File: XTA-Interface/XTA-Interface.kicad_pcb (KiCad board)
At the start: 2 copper layers, 99.9 x 99.9 mm, 19 parts, among them J1 XTA_CONNECTOR_0, J2 Drive Power, J3 Bus_ISA_8bit, J4 Addresses, J5 Addresses, J6 LEDs, J7 XTA_CONNECTOR_1, U1 BIOS FLASH, U2 74HCT245, U3 ATF/GAL16V8-15, U4 ATF/GAL16V8-15

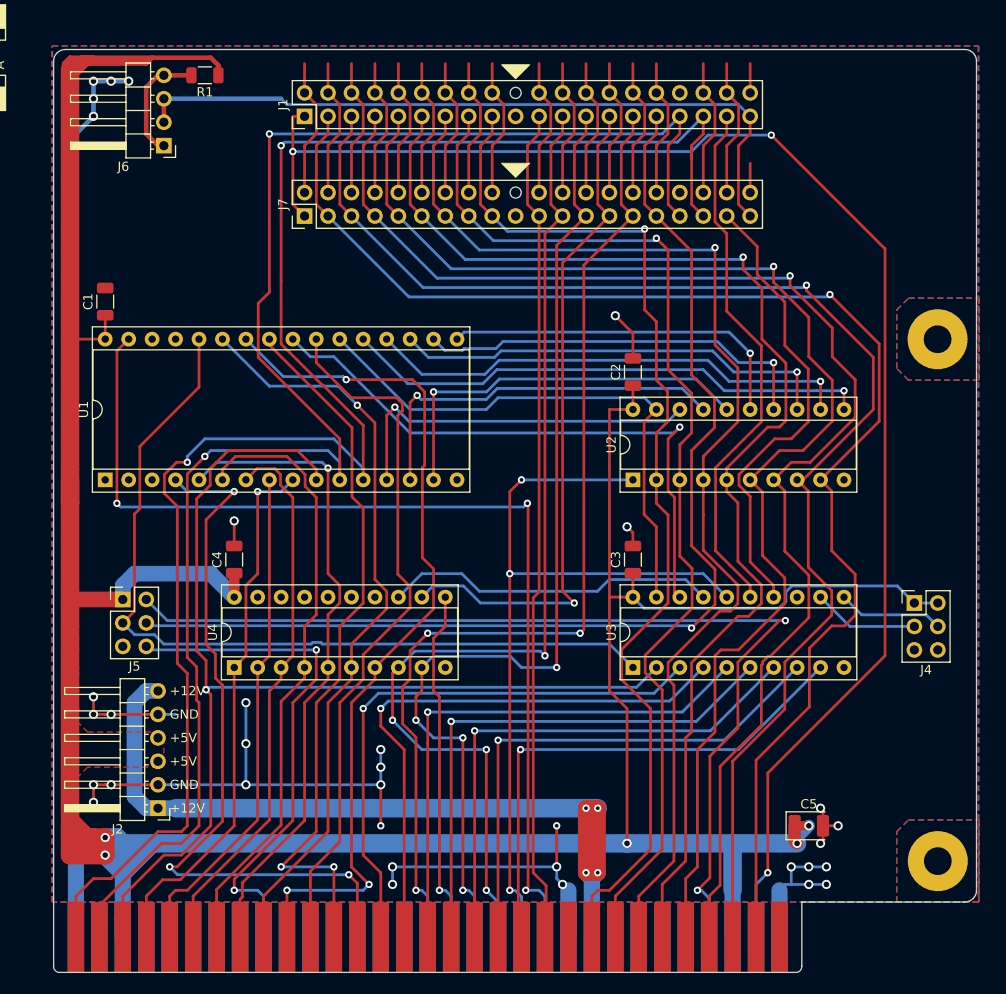
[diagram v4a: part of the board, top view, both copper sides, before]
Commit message: WIP on XTA interface layout.
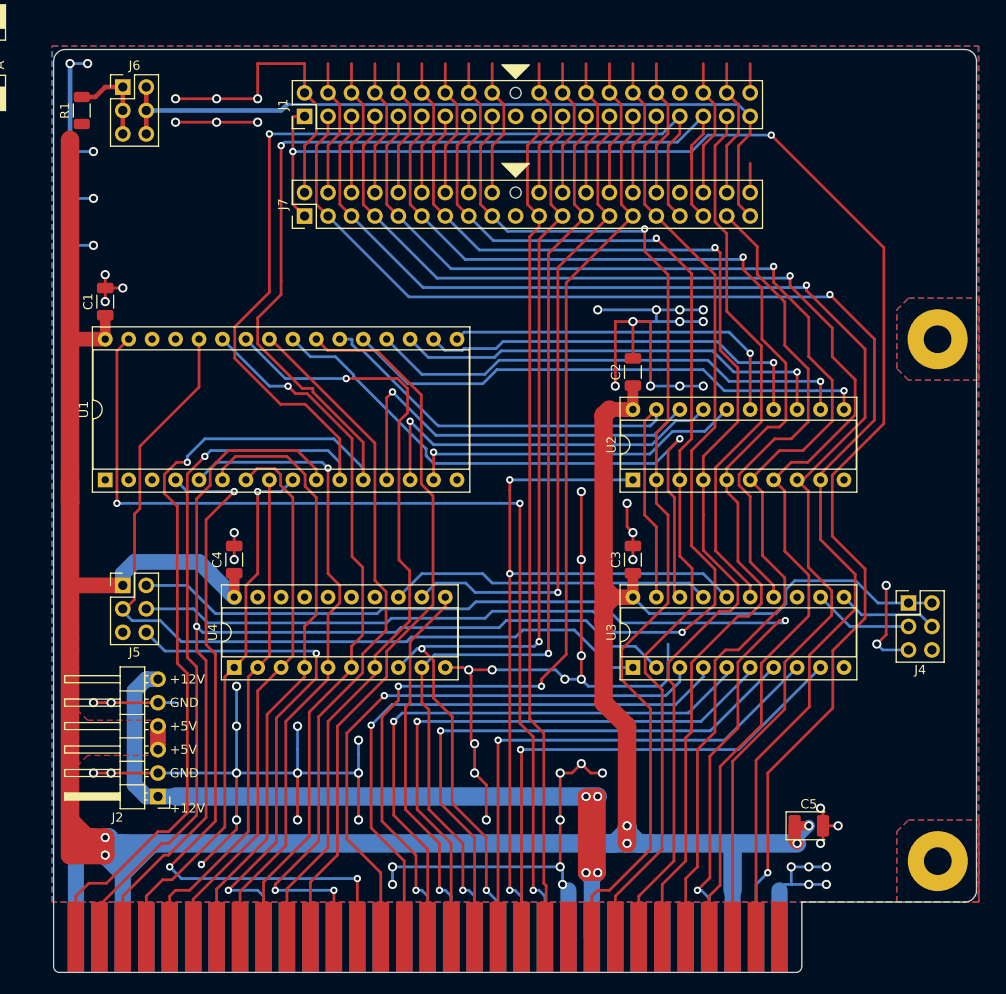
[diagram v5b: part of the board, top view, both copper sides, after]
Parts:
- J6: footprint Connector_PinHeader_2.54mm:PinHeader_1x04_P2.54mm_Horizontal -> Connector_PinHeader_2.54mm:PinHeader_2x03_P2.54mm_Vertical
- R1: value 1K -> 220R
- moved R1 13.9 mm to (99.7, 48.9), turned to 90 degrees
- moved J6 7.75 mm to (104.1, 46.4), turned to 0 degrees
- moved J5 1.52 mm to (104.1, 100.3)
- moved J2 1.27 mm to (108.0, 123.2)
- moved J4 0.64 mm to (189.2, 102.2)
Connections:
- J6 pad 3: ~DRV_ACTIVE -> Net-(J6-Pad1)
- J6 pad 4: Net-(J6-Pad1) -> ~DRV_ACTIVE
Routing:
- net GND: track 485.0 -> 674.2 mm, vias 34 -> 73
- net VCC: track 389.5 -> 356.8 mm, vias 5 -> 6
- net A09: track 94.4 -> 85.5 mm, vias 3 -> 1
- net D2_BUF: track 43.2 -> 36.8 mm
- net A16: track 58.2 -> 63.7 mm
- net ~IOW: track 115.4 -> 110.1 mm, vias 4 -> 3
- net A17: track 57.6 -> 62.8 mm
- net A15: track 58.8 -> 63.8 mm
- net ~IOR: track 112.0 -> 107.2 mm, vias 4 -> 2
- net A08: track 82.0 -> 77.4 mm
- net ~DRV_ACTIVE: track 78.7 -> 83.1 mm
- net D0_BUF: track 40.3 -> 44.0 mm
- net ~XTA_DACK: track 74.2 -> 70.7 mm
- net A11: track 78.4 -> 81.4 mm
- net Net-(J6-Pad1): track 12.9 -> 9.97 mm
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
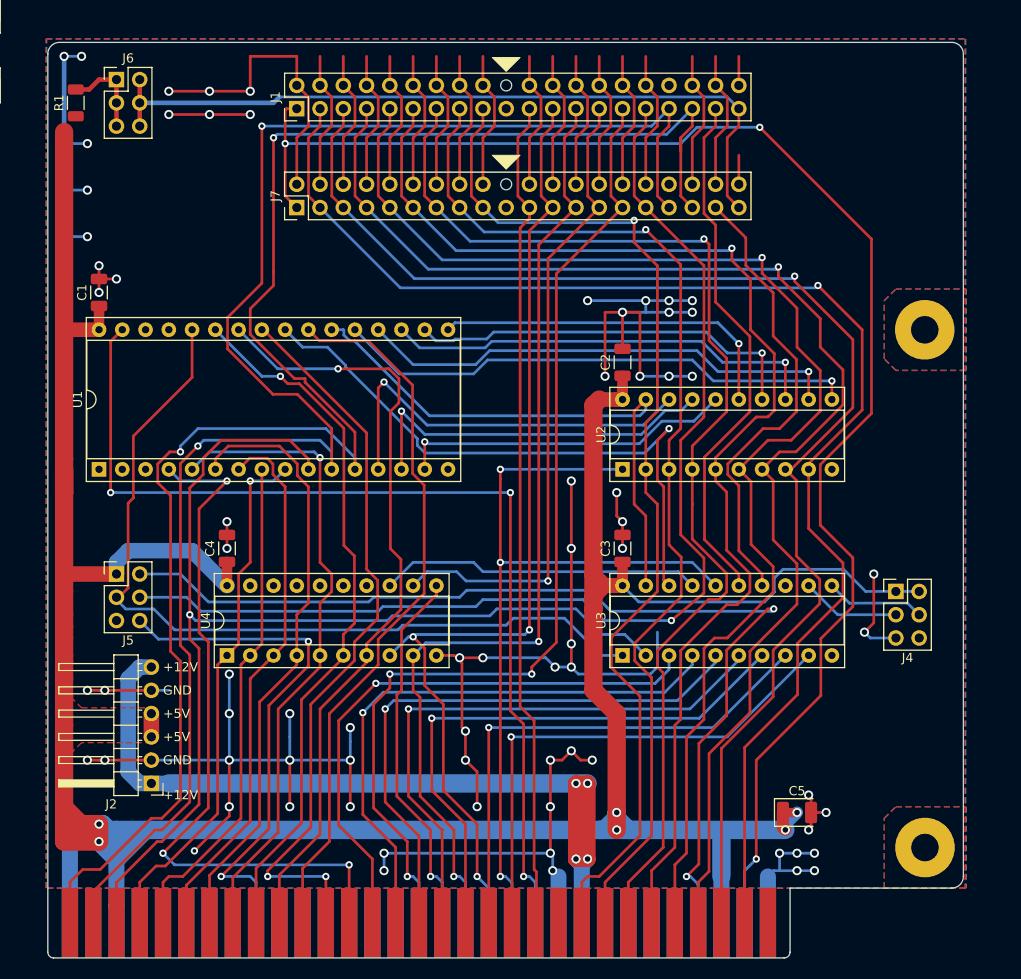
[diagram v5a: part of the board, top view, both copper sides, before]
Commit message: Finish first pass of layout of XTA interface card.
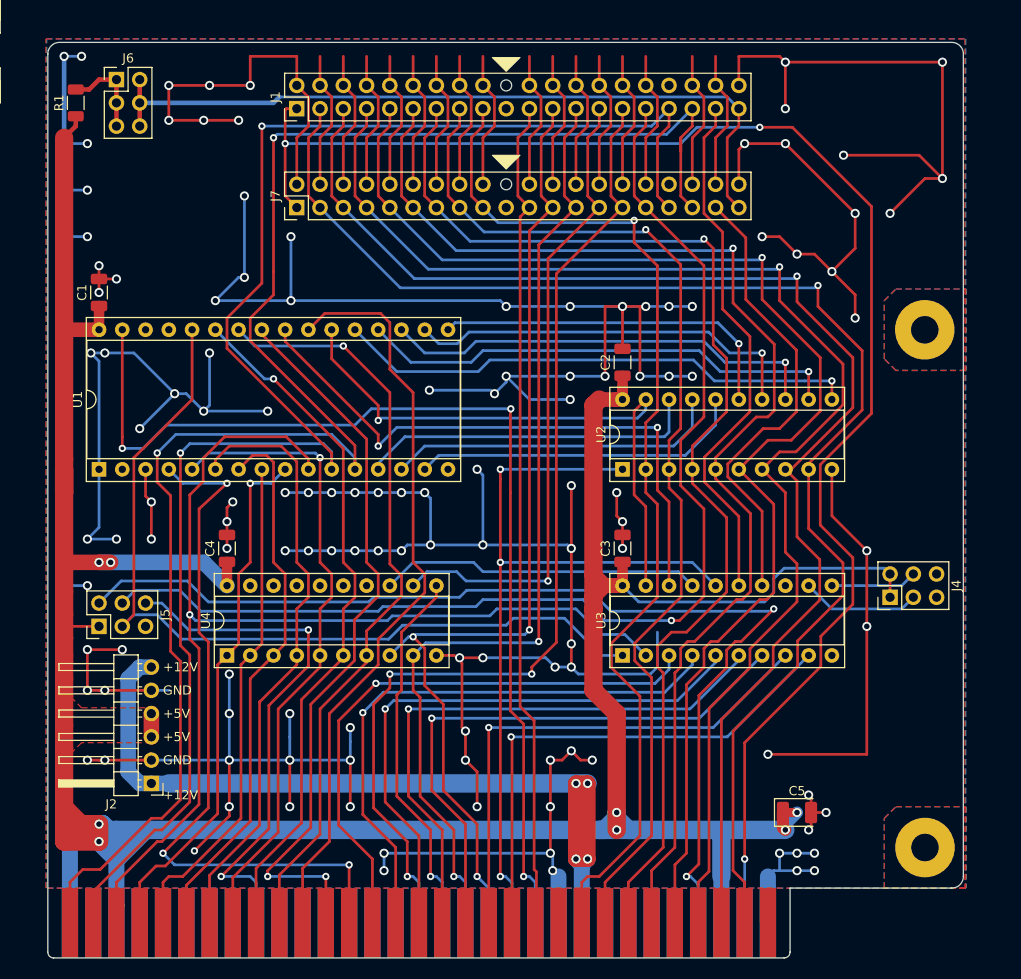
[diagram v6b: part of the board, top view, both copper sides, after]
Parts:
- moved J5 6.02 mm to (102.2, 106.0), turned to 90 degrees
- moved J4 0.90 mm to (188.6, 102.9), turned to 90 degrees
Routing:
- net GND: track 674.2 -> 1030.9 mm, vias 73 -> 127
- net D0_BUF: track 44.0 -> 37.4 mm, vias 1 -> 0
- net IRQ2: track 111.4 -> 116.6 mm
- net ~MEMW: track 110.4 -> 114.8 mm
- net A10: track 78.6 -> 82.7 mm
- net VCC: track 356.8 -> 360.9 mm, vias 6 -> 8
- net D1_BUF: track 40.7 -> 36.7 mm, vias 1 -> 0
- net XTA_IRQ: track 123.5 -> 126.6 mm
- net ~CE~_BIOS: track 61.3 -> 64.2 mm, vias 0 -> 1
- net ST_WD_JUMPER: track 91.7 -> 94.4 mm
- net A09: track 85.5 -> 83.3 mm
- net ADDR_JUMPER_0: track 10.8 -> 13.0 mm
- net RESET: track 165.7 -> 167.8 mm
- net ADDR_JUMPER_1: track 10.8 -> 9.42 mm
- net A08: track 77.4 -> 76.1 mm
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
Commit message: Silkscreen work for XTA interface.
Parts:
- removed the U4 at (116.2, 109.2)
- added U3: ATF/GAL16V8-15 "LEFT", Package_DIP:DIP-20_W7.62mm_Socket, F.Cu at (116.2, 109.2)
- CN1: renamed from J1; value XTA_CONNECTOR_0 -> DRIVE 0
- CN2: renamed from J7; value XTA_CONNECTOR_1 -> DRIVE 1
- JP1: renamed from J5; value Addresses -> Options
- U4: renamed from U3; value ATF/GAL16V8-15 -> ATF/GAL16V8-15 "RIGHT"
- renumbered C4 to C3, C3 to C4, J6 to CN3, J2 to CN4, J4 to JP2
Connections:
- JP2 pad 3: ADDR_JUMPER_0 -> ADDR_JUMPER_1
- JP2 pad 4: ADDR_JUMPER_1 -> ADDR_JUMPER_0
- U4 pad 11: ADDR_JUMPER_1 -> ADDR_JUMPER_0
- U4 pad 12: ADDR_JUMPER_0 -> ADDR_JUMPER_1
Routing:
- net VCC: track 360.9 -> 367.6 mm
- net GND: track 1030.9 -> 1024.5 mm, vias 127 -> 125
- net ADDR_JUMPER_1: track 9.42 -> 13.0 mm
- net ADDR_JUMPER_0: track 13.0 -> 9.42 mm
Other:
- board text added: "BIOS C800"
- board text added: "BIOS D000"
- board text added: "BIOS D800"
- board text added: "BIOS E000"
- board text added: "C"
- board text added: "D"
- board text added: "Drive Power"
- board text added: "IRQ 2"
- board text added: "IRQ 5"
- board text added: "MEGA XTA INTERFACE"
- board text added: "PRIMARY"
- board text added: "R1 is 1206 package C1-C4 are 1206 MLCC C5 is 3528 Tantalum"
- board text added: "SECONDARY"
- board text added: "Seagate ST05X compatible jumper settings:"
- board text added: "Set ST05X mode"
- board text added: "Set WDXT mode"
- board text added: "UNUSED"
- board text added: "WDXT notes: If IRQ 2 is selected, the WD drive must also be configured for IRQ 2. IRQ 2 is not supported on Seagate drives. When set to primary, BIOS address is C800 and port is 320. When set to secondary, BIOS address is CA00 and port is 322."
- board text added: "Western Digital WDXT-150 compatible jumper settings:"
- board text removed: "CF COMBO SUPER-LITE"
- board text removed: "Thanks to the XTIDE Universal BIOS Team and others who contributed to the XTIDE Universal BIOS. Additional thanks to Rob Krenicki, Jacob Dorne/Monotech PCs and James Pearce/Lo-tech for their influencing works."

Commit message: Finished first pass on board design.
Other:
- board text removed: "300h"
- board text removed: "320h"
- board text removed: "8086/8088"
- board text removed: "ABSENT"
- board text removed: "ATA PORT"
- board text removed: "BIOS"
- board text removed: "C800h"
- board text removed: "CPU TYPE"
- board text removed: "D000h"
- board text removed: "IRQ"
- board text removed: "JUMPERS"
- board text removed: "PRESENT"
- board text removed: "ROM ADDR"
- board text removed: "ROM ADDR 0"
- board text removed: "ROM ADDR 1"
- board text removed: "RTC OPTION"
- board text removed: "V20, 286,..."
